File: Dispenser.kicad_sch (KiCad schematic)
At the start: 10 parts, among them P1 Conn_01x02, U1 TMC2208_SILENTSTEPSTICK

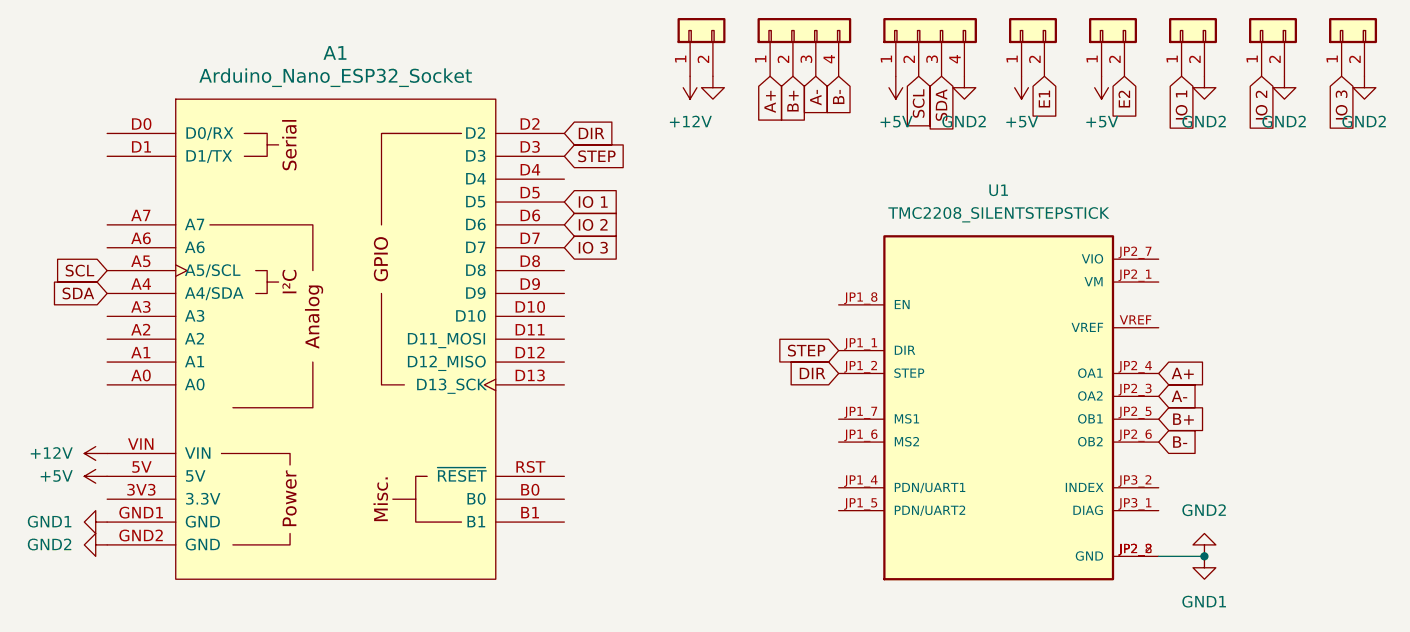
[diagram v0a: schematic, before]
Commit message: Update Schematic and Finsh Board
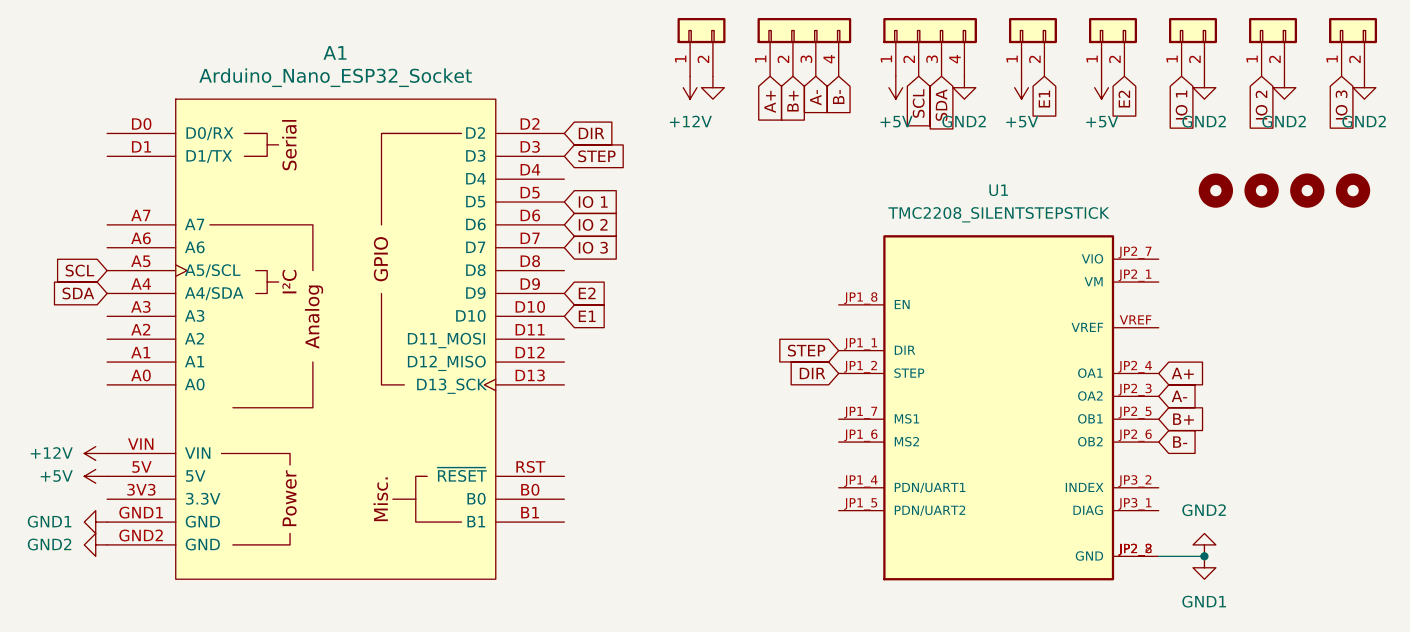
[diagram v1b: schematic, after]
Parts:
- added H1, H2, H3, H4: MountingHole, symbol Mechanical:MountingHole
- IO3: footprint Connector_JST:JST_EH_B4B-EH-A_1x04_P2.50mm_Vertical -> Connector_JST:JST_EH_B2B-EH-A_1x02_P2.50mm_Vertical
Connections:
- net E1: now also A1.D10
- net E2: now also A1.D9
